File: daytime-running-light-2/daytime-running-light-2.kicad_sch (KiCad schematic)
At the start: 58 parts, among them J1 Conn_01x01_Socket, J2 Conn_01x01_Socket, J3 Conn_01x01_Socket, J4 Conn_01x01_Socket, J5 Conn_01x01_Socket, J6 Conn_01x01_Pin, J7 Conn_01x01_Socket, J8 Conn_01x01_Socket, J9 Conn_01x01_Socket, Q1 BC548, Q2 IRF9540N, Q3 IRFB3004PbF, SW1 SW_SPST, U1 L7812, U2 TLC555xP, U3 L7812, U4 4001, U5 4069, U6 IRS10752LPbF

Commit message: [DRL] Fix and update PCB and schematic  Use BAT2 and VCC2  Add missing net on PCB  Improve zones for BAT2 and GND2
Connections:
- net VCC_STAB is gone; now on net VCC: C4.1, C8.1, C9.1, R4.2, U1.3 (OUT), U4.14 (VDD), U5.14 (VDD)
- net VCC: no longer J1.1 (Pin_1), SW1.1 (A)
- net +12V renamed +BATT2
- net VCC_STAB2 renamed VCC2
- new net +BATT: J1.1 (Pin_1), SW1.1 (A)

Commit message: [DRL] Improve schematic and PCB
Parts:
- D3, D4: value 1.5KExxA -> 1.5KE18A
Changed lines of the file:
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@@
       (effects (font (size 1.27 1.27)) (justify left))
     )
-    (property "Value" "1.5KExxA" (at 97.79 122.555 90)
+    (property "Value" "1.5KE18A" (at 97.79 122.555 90)
       (effects (font (size 1.27 1.27)) (justify left))
     )
@@
       (effects (font (size 1.27 1.27)) (justify left))
     )
-    (property "Value" "1.5KExxA" (at 97.79 107.95 90)
-      (effects (font (size 1.27 1.27)) (justify left))
-    )
+    (property "Value" "1.5KE18A" (at 97.79 107.95 90)
+      (effects (font (size 1.27 1.27)) (justify left))
+    )

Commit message: [drl] Add proper voltage bootstrap powered from a double voltage. Start reimpl PCB
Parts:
- removed C10: C, Capacitor_THT:C_Disc_D5.0mm_W2.5mm_P5.00mm, symbol Device:C
- removed D2: 1N4148, Diode_THT:D_DO-35_SOD27_P5.08mm_Vertical_KathodeUp, symbol Diode:1N4148
- added C10: 4.7uF, Capacitor_THT:CP_Radial_D5.0mm_P2.00mm, symbol Device:C_Polarized
- added C11, C8: 100nF, Capacitor_THT:C_Disc_D6.0mm_W2.5mm_P5.00mm, symbol Device:C
- added C9: 1uF, Capacitor_THT:CP_Radial_D5.0mm_P2.00mm, symbol Device:C_Polarized
- added D2, D3: BAT42, Diode_THT:D_DO-35_SOD27_P5.08mm_Vertical_KathodeUp, symbol Diode:BAT42
- added D4: 1N4746A, 18V, Diode_THT:D_DO-41_SOD81_P3.81mm_Vertical_KathodeUp, symbol Diode:1N47xxA
- added D5: 1N4148, Diode_THT:D_DO-35_SOD27_P7.62mm_Horizontal, symbol Diode:1N4148
- added R18: 0R, Resistor_THT:R_Axial_DIN0207_L6.3mm_D2.5mm_P7.62mm_Horizontal, symbol Device:R
- added R2: 1k, Resistor_THT:R_Axial_DIN0207_L6.3mm_D2.5mm_P2.54mm_Vertical, symbol Device:R
- added R4: 51, Resistor_THT:R_Axial_DIN0207_L6.3mm_D2.5mm_P2.54mm_Vertical, symbol Device:R
- R5: renamed from R3; footprint Resistor_THT:R_Axial_DIN0207_L6.3mm_D2.5mm_P2.54mm_Vertical -> Resistor_THT:R_Axial_DIN0207_L6.3mm_D2.5mm_P7.62mm_Horizontal
- renumbered C8 to C12, C9 to C13, C11 to C14, C12 to C15, D7 to D10, D3 to D6, D4 to D7, D5 to D8, D6 to D9, J9 to J2, J2 to J3, J8 to J4, J3 to J5, J4 to J6, J5 to J7, J6 to J8, J7 to J9, R8 to R10, R9 to R11, R10 to R12, R11 to R13, R12 to R14, R13 to R15, R14 to R16, R2 to R3, R4 to R6, R5 to R7, R6 to R8, R7 to R9
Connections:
- net +BATT2: now also D2.2 (A)
- net GND2: now also C9.2, D4.2 (A)
- net PWM: now also C8.2
- net at U6.6 (VB): now also R18.1
- net POWER_OUTPUT renamed GND3
- net GND3: now also C10.2, C11.2
- new net: D5.1 (K), R4.1
- new net: C8.1, D2.1 (K), D3.2 (A)
- new net: C9.1, D3.1 (K), R2.1
- new net DOUBLED_VCC2: D4.1 (K), D5.2 (A), R2.2
- new net V_BOOTSTRAP: C10.1, C11.1, R18.2, R4.2
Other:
- note added: "J6 pin voltage: - logical low - allow PWM circuitry power on - logical high - disallow PWM circuitry power on GND3 isn't really a ground connection."

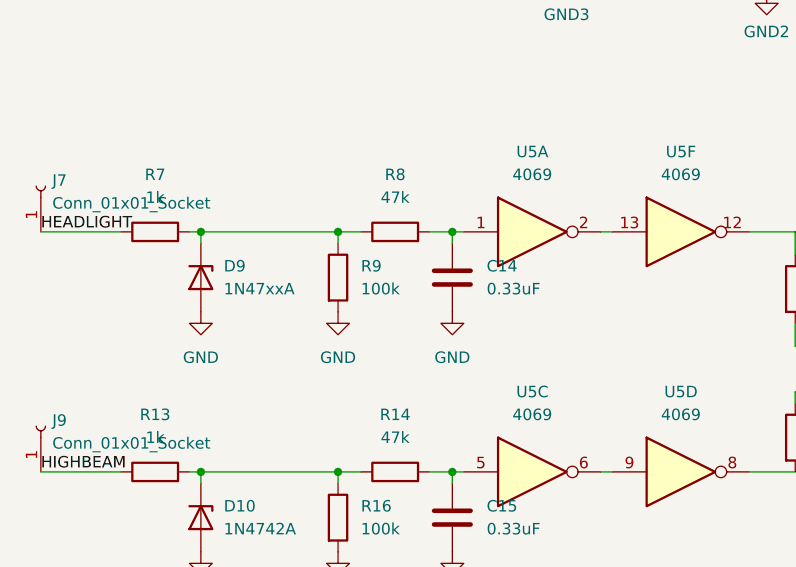
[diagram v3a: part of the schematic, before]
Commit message: [drl] Finish PCB.
    TODO - fix DRC.
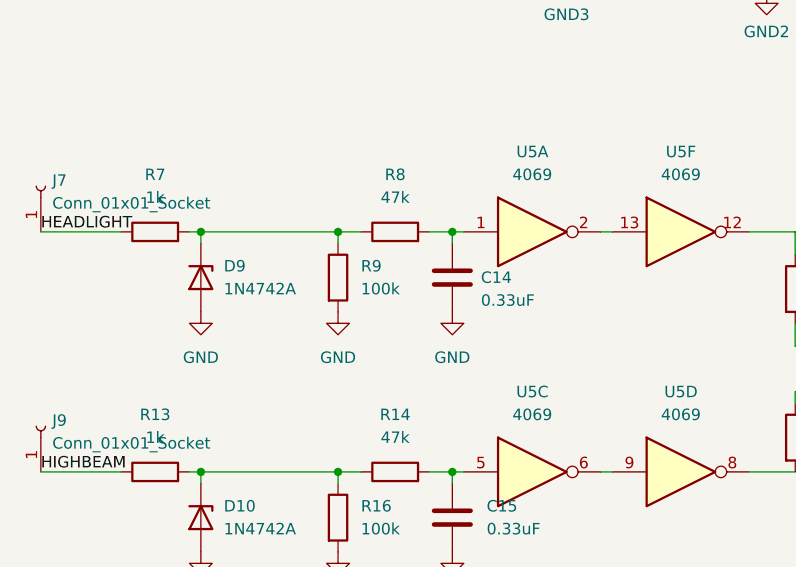
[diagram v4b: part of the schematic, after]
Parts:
- D9: value 1N47xxA -> 1N4742A
- R11: footprint Resistor_THT:R_Axial_DIN0207_L6.3mm_D2.5mm_P2.54mm_Vertical -> Resistor_THT:R_Axial_DIN0207_L6.3mm_D2.5mm_P7.62mm_Horizontal
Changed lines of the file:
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@@
       (effects (font (size 1.27 1.27)) (justify left))
     )
-    (property "Value" "1N47xxA" (at 34.925 160.02 90)
+    (property "Value" "1N4742A" (at 34.925 160.02 90)
       (effects (font (size 1.27 1.27)) (justify left))
     )
@@
   )
   (symbol (lib_id "Device:C") (at 60.325 158.75 0) (unit 1)
-    (in_bom yes) (on_board yes) (dnp no) (fields_autoplaced)
-    (property "Reference" "C14" (at 64.135 157.48 0)
-      (effects (font (size 1.27 1.27)) (justify left))
-    )
-    (property "Value" "0.33uF" (at 64.135 160.02 0)
+    (in_bom yes) (on_board yes) (dnp no)
+    (property "Reference" "C14" (at 63.5 158.75 0)
+      (effects (font (size 1.27 1.27)) (justify left))
+    )
+    (property "Value" "0.33uF" (at 63.5 161.29 0)
       (effects (font (size 1.27 1.27)) (justify left))
     )
@@
       (effects (font (size 1.27 1.27)))
     )
-    (property "Footprint" "Resistor_THT:R_Axial_DIN0207_L6.3mm_D2.5mm_P2.54mm_Vertical" (at 146.685 170.688 90)
-      (effects (font (size 1.27 1.27)) hide)
-    )
+    (property "Footprint" "Resistor_THT:R_Axial_DIN0207_L6.3mm_D2.5mm_P7.62mm_Horizontal" (at 146.685 170.688 90)
+      (effects (font (size 1.27 1.27)) hide)
+    )

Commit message: [drl] Fix design rules check
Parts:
- D3: footprint Diode_THT:D_DO-35_SOD27_P5.08mm_Vertical_KathodeUp -> Diode_THT:D_DO-35_SOD27_P5.08mm_Vertical_AnodeUp
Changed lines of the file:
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@@
       (effects (font (size 1.27 1.27)))
     )
-    (property "Footprint" "Diode_THT:D_DO-35_SOD27_P5.08mm_Vertical_KathodeUp" (at 137.16 71.12 0)
+    (property "Footprint" "Diode_THT:D_DO-35_SOD27_P5.08mm_Vertical_AnodeUp" (at 137.16 71.12 0)
       (effects (font (size 1.27 1.27)) hide)
     )

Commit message: [drl] Update some zones and traces on PCB. Fix DRC. Reduce size of ctrl PCB. Add zones for headlight and highbeam connection.
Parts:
- D9: footprint Diode_THT:D_DO-41_SOD81_P10.16mm_Horizontal -> Diode_THT:D_DO-41_SOD81_P3.81mm_Vertical_KathodeUp
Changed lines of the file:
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@@
       (effects (font (size 1.27 1.27)) (justify left))
     )
-    (property "Footprint" "Diode_THT:D_DO-41_SOD81_P10.16mm_Horizontal" (at 27.94 158.75 0)
+    (property "Footprint" "Diode_THT:D_DO-41_SOD81_P3.81mm_Vertical_KathodeUp" (at 27.94 158.75 0)
       (effects (font (size 1.27 1.27)) hide)
     )
